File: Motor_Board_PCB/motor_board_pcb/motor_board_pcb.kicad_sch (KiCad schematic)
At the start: 0 parts

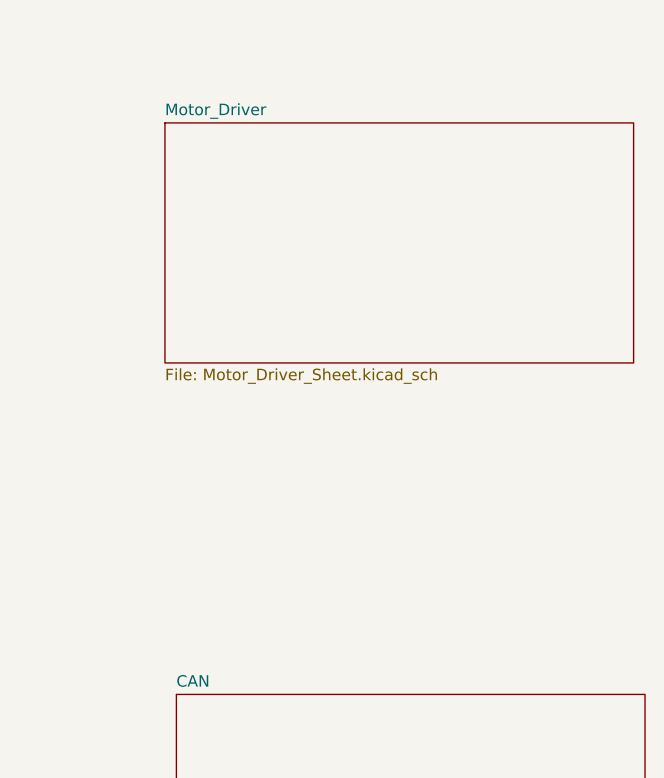
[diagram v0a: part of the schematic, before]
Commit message: Integrated MCU to Motor board
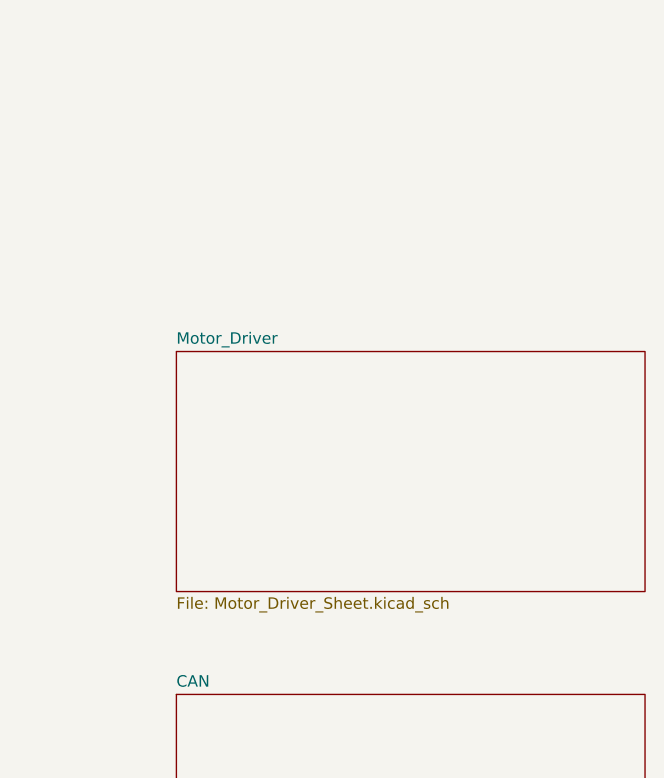
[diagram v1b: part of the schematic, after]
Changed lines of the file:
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@@
     )
   )
-  (sheet (at 203.2 45.72) (size 52.07 26.67) (fields_autoplaced)
+  (sheet (at 204.47 71.12) (size 52.07 26.67) (fields_autoplaced)
     (stroke (width 0.1524) (type solid))
     (fill (color 0 0 0 0.0000))
-    (property "Sheetname" "Motor_Driver" (at 203.2 45.0084 0)
+    (property "Sheetname" "Motor_Driver" (at 204.47 70.4084 0)
       (effects (font (size 1.27 1.27)) (justify left bottom))
     )
-    (property "Sheetfile" "Motor_Driver_Sheet.kicad_sch" (at 203.2 72.9746 0)
+    (property "Sheetfile" "Motor_Driver_Sheet.kicad_sch" (at 204.47 98.3746 0)
       (effects (font (size 1.27 1.27)) (justify left top))
     )

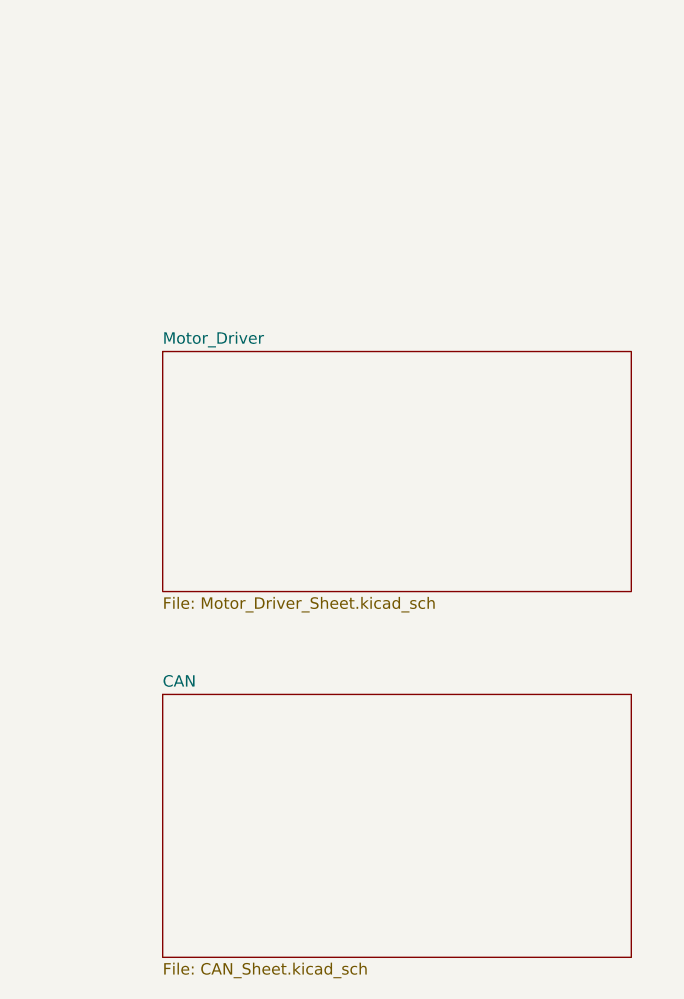
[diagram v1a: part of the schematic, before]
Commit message: Added power and motor driver chip schematics
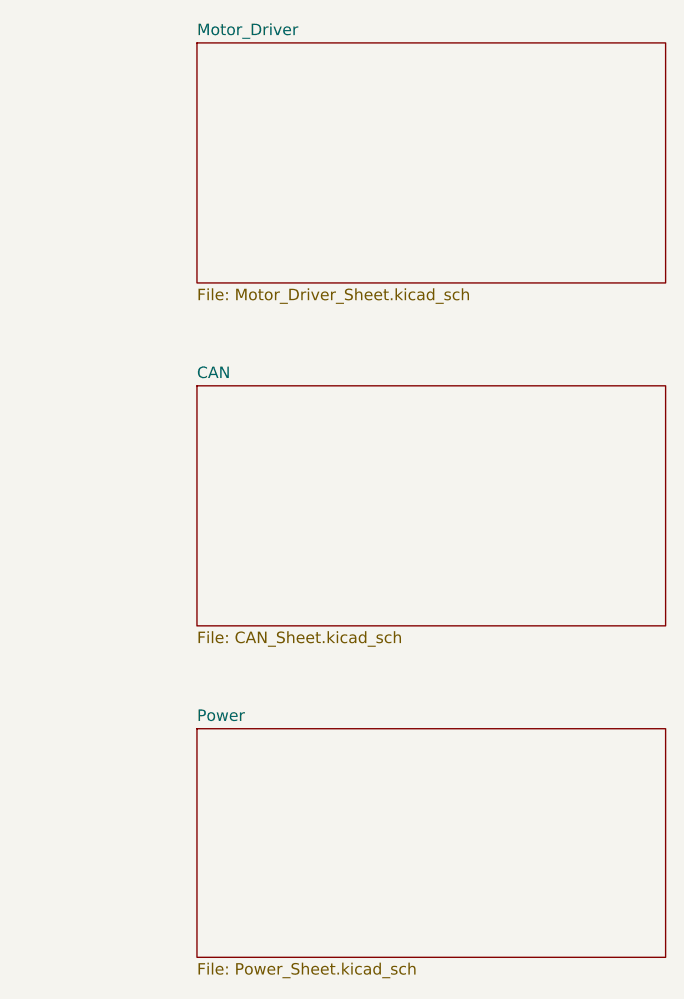
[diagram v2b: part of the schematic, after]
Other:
- added sheet Power (Power_Sheet.kicad_sch)
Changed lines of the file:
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@@
 (kicad_sch (version 20230121) (generator eeschema)
   (paper "A4")
-  (sheet (at 204.47 109.22) (size 52.07 29.21) (fields_autoplaced)
+  (sheet (at 208.28 74.93) (size 52.07 26.67) (fields_autoplaced)
     (stroke (width 0.1524) (type solid))
     (fill (color 0 0 0 0.0000))
-    (property "Sheetname" "CAN" (at 204.47 108.5084 0)
+    (property "Sheetname" "CAN" (at 208.28 74.2184 0)
       (effects (font (size 1.27 1.27)) (justify left bottom))
     )
-    (property "Sheetfile" "CAN_Sheet.kicad_sch" (at 204.47 139.0146 0)
+    (property "Sheetfile" "CAN_Sheet.kicad_sch" (at 208.28 102.1846 0)
       (effects (font (size 1.27 1.27)) (justify left top))
     )
@@
     )
   )
-  (sheet (at 204.47 71.12) (size 52.07 26.67) (fields_autoplaced)
+  (sheet (at 208.28 113.03) (size 52.07 25.4) (fields_autoplaced)
     (stroke (width 0.1524) (type solid))
     (fill (color 0 0 0 0.0000))
-    (property "Sheetname" "Motor_Driver" (at 204.47 70.4084 0)
+    (property "Sheetname" "Power" (at 208.28 112.3184 0)
       (effects (font (size 1.27 1.27)) (justify left bottom))
     )
-    (property "Sheetfile" "Motor_Driver_Sheet.kicad_sch" (at 204.47 98.3746 0)
+    (property "Sheetfile" "Power_Sheet.kicad_sch" (at 208.28 139.0146 0)
       (effects (font (size 1.27 1.27)) (justify left top))
     )
+    (instances
+      (project "motor_board_pcb"
+        (path "/4ad82a24-c992-45c9-b523-12e12bcd6ced" (page "5"))
+      )
+    )
+  )
+  (sheet (at 208.28 36.83) (size 52.07 26.67) (fields_autoplaced)
+    (stroke (width 0.1524) (type solid))
+    (fill (color 0 0 0 0.0000))
+    (property "Sheetname" "Motor_Driver" (at 208.28 36.1184 0)
+      (effects (font (size 1.27 1.27)) (justify left bottom))
+    )
+    (property "Sheetfile" "Motor_Driver_Sheet.kicad_sch" (at 208.28 64.0846 0)
+      (effects (font (size 1.27 1.27)) (justify left top))
+    )

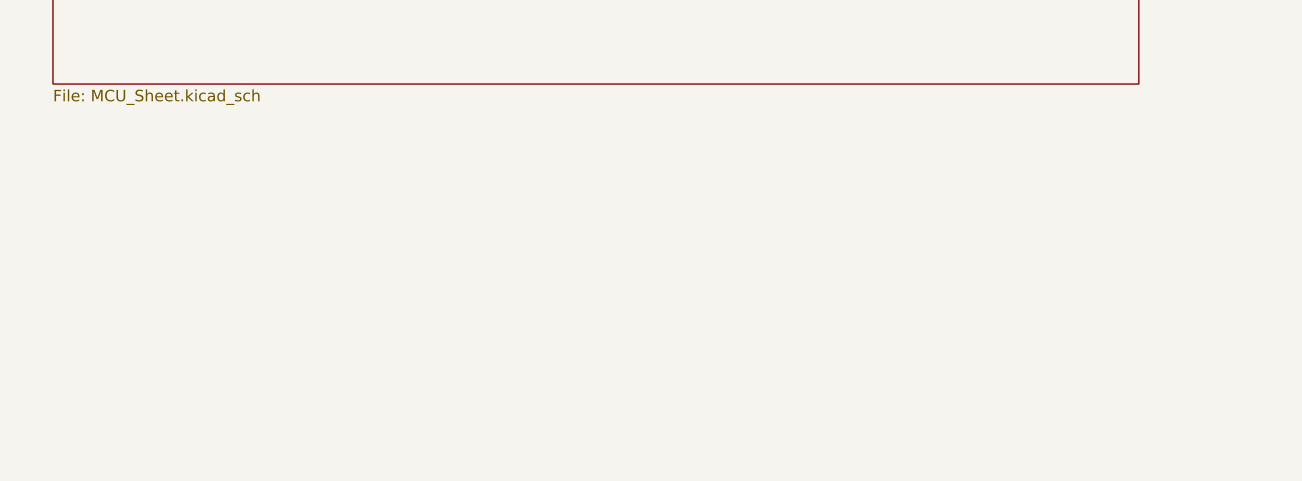
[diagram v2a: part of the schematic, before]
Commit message: Added footprints for almost all components
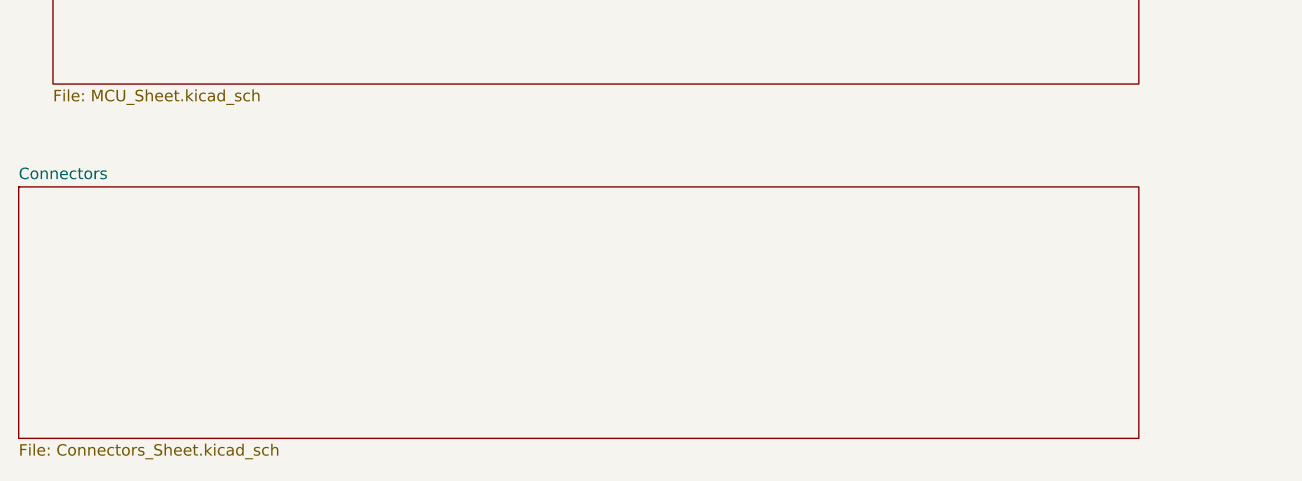
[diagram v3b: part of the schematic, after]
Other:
- added sheet Connectors (Connectors_Sheet.kicad_sch)
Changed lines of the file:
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@@
+    )
+  )
+  (sheet (at 24.13 149.86) (size 124.46 27.94) (fields_autoplaced)
+    (stroke (width 0.1524) (type solid))
+    (fill (color 0 0 0 0.0000))
+    (property "Sheetname" "Connectors" (at 24.13 149.1484 0)
+      (effects (font (size 1.27 1.27)) (justify left bottom))
+    )
+    (property "Sheetfile" "Connectors_Sheet.kicad_sch" (at 24.13 178.3846 0)
+      (effects (font (size 1.27 1.27)) (justify left top))
+    )
+    (instances
+      (project "motor_board_pcb"
+        (path "/4ad82a24-c992-45c9-b523-12e12bcd6ced" (page "6"))
+      )
     )
   )
